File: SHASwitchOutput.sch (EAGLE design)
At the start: 39 parts, among them IC2 HLKPM01, Q1 2N7002, Q2 2N7002, Q3 2N7002, Q4 2N7002

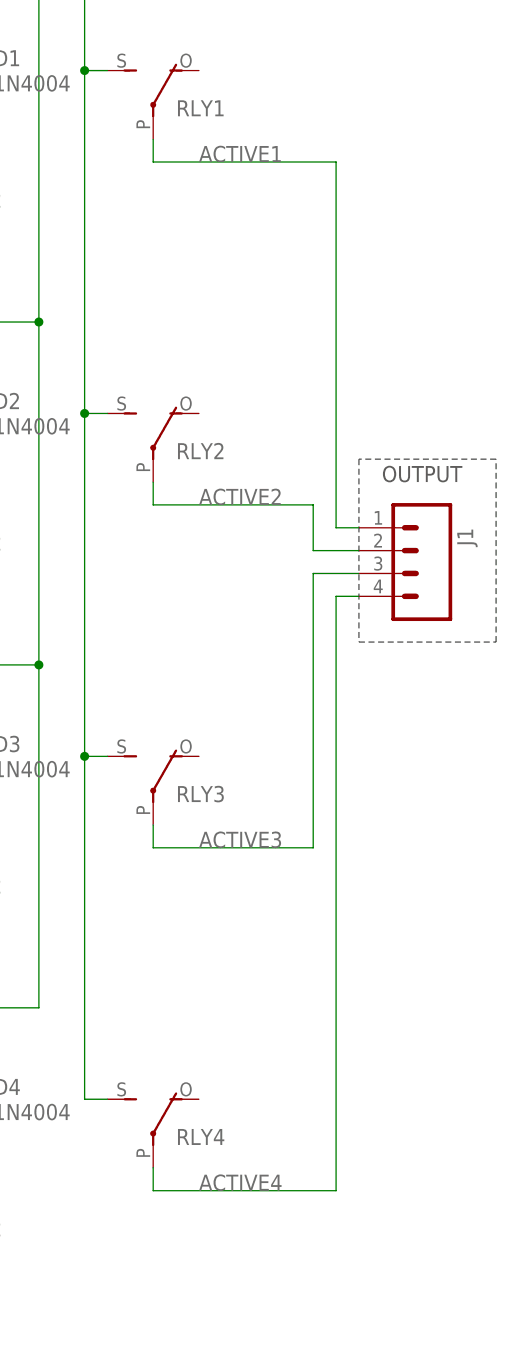
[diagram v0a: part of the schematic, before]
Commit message: Changed screw terminals from 3.5mm pitch to 5mm
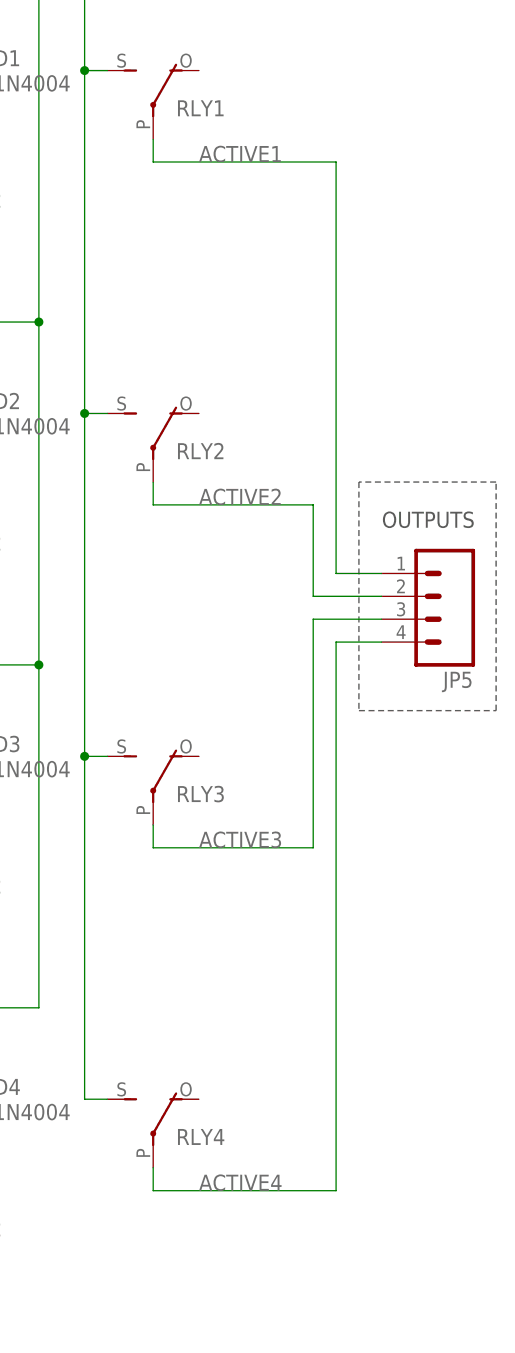
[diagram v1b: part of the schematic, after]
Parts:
- removed J1: (no value), freetronics-master-v1.1:M04SCREW
- added JP5: (no value), freetronics-jon:M045MM
- JP2: device freetronics-original:M03SCREW -> freetronics-jon:M035MM
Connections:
- net ACTIVE1: now also JP5.1; no longer J1.1
- net ACTIVE2: now also JP5.2; no longer J1.2
- net ACTIVE3: now also JP5.3; no longer J1.3
- net ACTIVE4: now also JP5.4; no longer J1.4
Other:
- note added: "OUTPUTS"
- note removed: "OUTPUT"
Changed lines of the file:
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@@
 <part name="GND12" library="SparkFun" deviceset="GND" device=""/>
 <part name="IC2" library="freetronics-jon" deviceset="HLKPM01" device=""/>
-<part name="J1" library="freetronics-master-v1.1" deviceset="M04" device="SCREW"/>
 <part name="GND2" library="SparkFun" deviceset="GND" device=""/>
 <part name="R2" library="freetronics" deviceset="RESISTOR" device="0603" value="330R"/>
@@
 <part name="JP1" library="freetronics-original" deviceset="M10" device="0.1"/>
 <part name="F1" library="freetronics-jon" deviceset="PICOFUSE" device="" value="250V 1A"/>
-<part name="JP2" library="freetronics-original" deviceset="M03" device="SCREW"/>
+<part name="JP2" library="freetronics-jon" deviceset="M03" device="5MM"/>
 <part name="GND14" library="SparkFun" deviceset="GND" device=""/>
 <part name="U$3" library="freetronics-original" deviceset="5V" device=""/>
+<part name="JP5" library="freetronics-jon" deviceset="M04" device="5MM"/>
 </parts>
 <sheets>
@@
 <frame x1="78.74" y1="5.08" x2="109.22" y2="10.16" columns="8" rows="5" layer="94"/>
 <frame x1="5.08" y1="5.08" x2="30.48" y2="10.16" columns="8" rows="5" layer="94"/>
-<wire x1="243.84" y1="114.3" x2="228.6" y2="114.3" width="0.1524" layer="97" style="shortdash"/>
-<wire x1="228.6" y1="114.3" x2="228.6" y2="93.98" width="0.1524" layer="97" style="shortdash"/>
-<wire x1="228.6" y1="93.98" x2="243.84" y2="93.98" width="0.1524" layer="97" style="shortdash"/>
-<wire x1="243.84" y1="93.98" x2="243.84" y2="114.3" width="0.1524" layer="97" style="shortdash"/>
-<text x="231.14" y="111.76" size="1.778" layer="97">OUTPUT</text>
+<wire x1="243.84" y1="111.76" x2="228.6" y2="111.76" width="0.1524" layer="97" style="shortdash"/>
+<wire x1="228.6" y1="111.76" x2="228.6" y2="86.36" width="0.1524" layer="97" style="shortdash"/>
+<wire x1="228.6" y1="86.36" x2="243.84" y2="86.36" width="0.1524" layer="97" style="shortdash"/>
+<wire x1="243.84" y1="86.36" x2="243.84" y2="111.76" width="0.1524" layer="97" style="shortdash"/>
+<text x="231.14" y="106.68" size="1.778" layer="97">OUTPUTS</text>
 </plain>
 <instances>
@@
 <instance part="GND12" gate="1" x="165.1" y="91.44"/>
 <instance part="IC2" gate="G$1" x="71.12" y="162.56"/>
-<instance part="J1" gate="G$1" x="233.68" y="104.14" smashed="yes" rot="R180">
-<attribute name="VALUE" x="238.76" y="111.76" size="1.778" layer="96" rot="R180"/>
-<attribute name="NAME" x="239.522" y="106.68" size="1.778" layer="95" rot="R270"/>
-</instance>
 <instance part="GND2" gate="1" x="137.16" y="48.26"/>
 <instance part="R2" gate="G$1" x="137.16" y="55.88" smashed="yes" rot="R90">
@@
 <instance part="GND14" gate="1" x="101.6" y="60.96"/>
 <instance part="U$3" gate="G$1" x="101.6" y="93.98"/>
+<instance part="JP5" gate="G$1" x="236.22" y="99.06" rot="R180"/>
 </instances>
 <busses>
@@
 <wire x1="205.74" y1="147.32" x2="205.74" y2="149.86" width="0.1524" layer="91"/>
 <label x="210.82" y="147.32" size="1.778" layer="95"/>
-<wire x1="226.06" y1="147.32" x2="226.06" y2="106.68" width="0.1524" layer="91"/>
-<pinref part="J1" gate="G$1" pin="1"/>
-<wire x1="226.06" y1="106.68" x2="228.6" y2="106.68" width="0.1524" layer="91"/>
+<wire x1="226.06" y1="147.32" x2="226.06" y2="101.6" width="0.1524" layer="91"/>
+<wire x1="231.14" y1="101.6" x2="226.06" y2="101.6" width="0.1524" layer="91"/>
+<pinref part="JP5" gate="G$1" pin="1"/>
 </segment>
 </net>
@@
 <wire x1="205.74" y1="109.22" x2="205.74" y2="111.76" width="0.1524" layer="91"/>
 <label x="210.82" y="109.22" size="1.778" layer="95"/>
-<wire x1="223.52" y1="109.22" x2="223.52" y2="104.14" width="0.1524" layer="91"/>
-<pinref part="J1" gate="G$1" pin="2"/>
-<wire x1="223.52" y1="104.14" x2="228.6" y2="104.14" width="0.1524" layer="91"/>
+<wire x1="223.52" y1="109.22" x2="223.52" y2="99.06" width="0.1524" layer="91"/>
+<wire x1="223.52" y1="99.06" x2="231.14" y2="99.06" width="0.1524" layer="91"/>
+<pinref part="JP5" gate="G$1" pin="2"/>
 </segment>
 </net>
@@
 <wire x1="205.74" y1="71.12" x2="205.74" y2="73.66" width="0.1524" layer="91"/>
 <label x="210.82" y="71.12" size="1.778" layer="95"/>
-<wire x1="223.52" y1="71.12" x2="223.52" y2="101.6" width="0.1524" layer="91"/>
-<pinref part="J1" gate="G$1" pin="3"/>
-<wire x1="223.52" y1="101.6" x2="228.6" y2="101.6" width="0.1524" layer="91"/>
+<wire x1="223.52" y1="71.12" x2="223.52" y2="96.52" width="0.1524" layer="91"/>
+<wire x1="223.52" y1="96.52" x2="231.14" y2="96.52" width="0.1524" layer="91"/>
+<pinref part="JP5" gate="G$1" pin="3"/>
 </segment>
 </net>
@@
 <wire x1="205.74" y1="33.02" x2="205.74" y2="35.56" width="0.1524" layer="91"/>
 <label x="210.82" y="33.02" size="1.778" layer="95"/>
-<wire x1="226.06" y1="33.02" x2="226.06" y2="99.06" width="0.1524" layer="91"/>
-<pinref part="J1" gate="G$1" pin="4"/>
-<wire x1="226.06" y1="99.06" x2="228.6" y2="99.06" width="0.1524" layer="91"/>
-</segment>
-</net>
+<wire x1="226.06" y1="33.02" x2="226.06" y2="93.98" width="0.1524" layer="91"/>
+<wire x1="226.06" y1="93.98" x2="231.14" y2="93.98" width="0.1524" layer="91"/>
+<pinref part="JP5" gate="G$1" pin="4"/>
+</segment>
+</net>

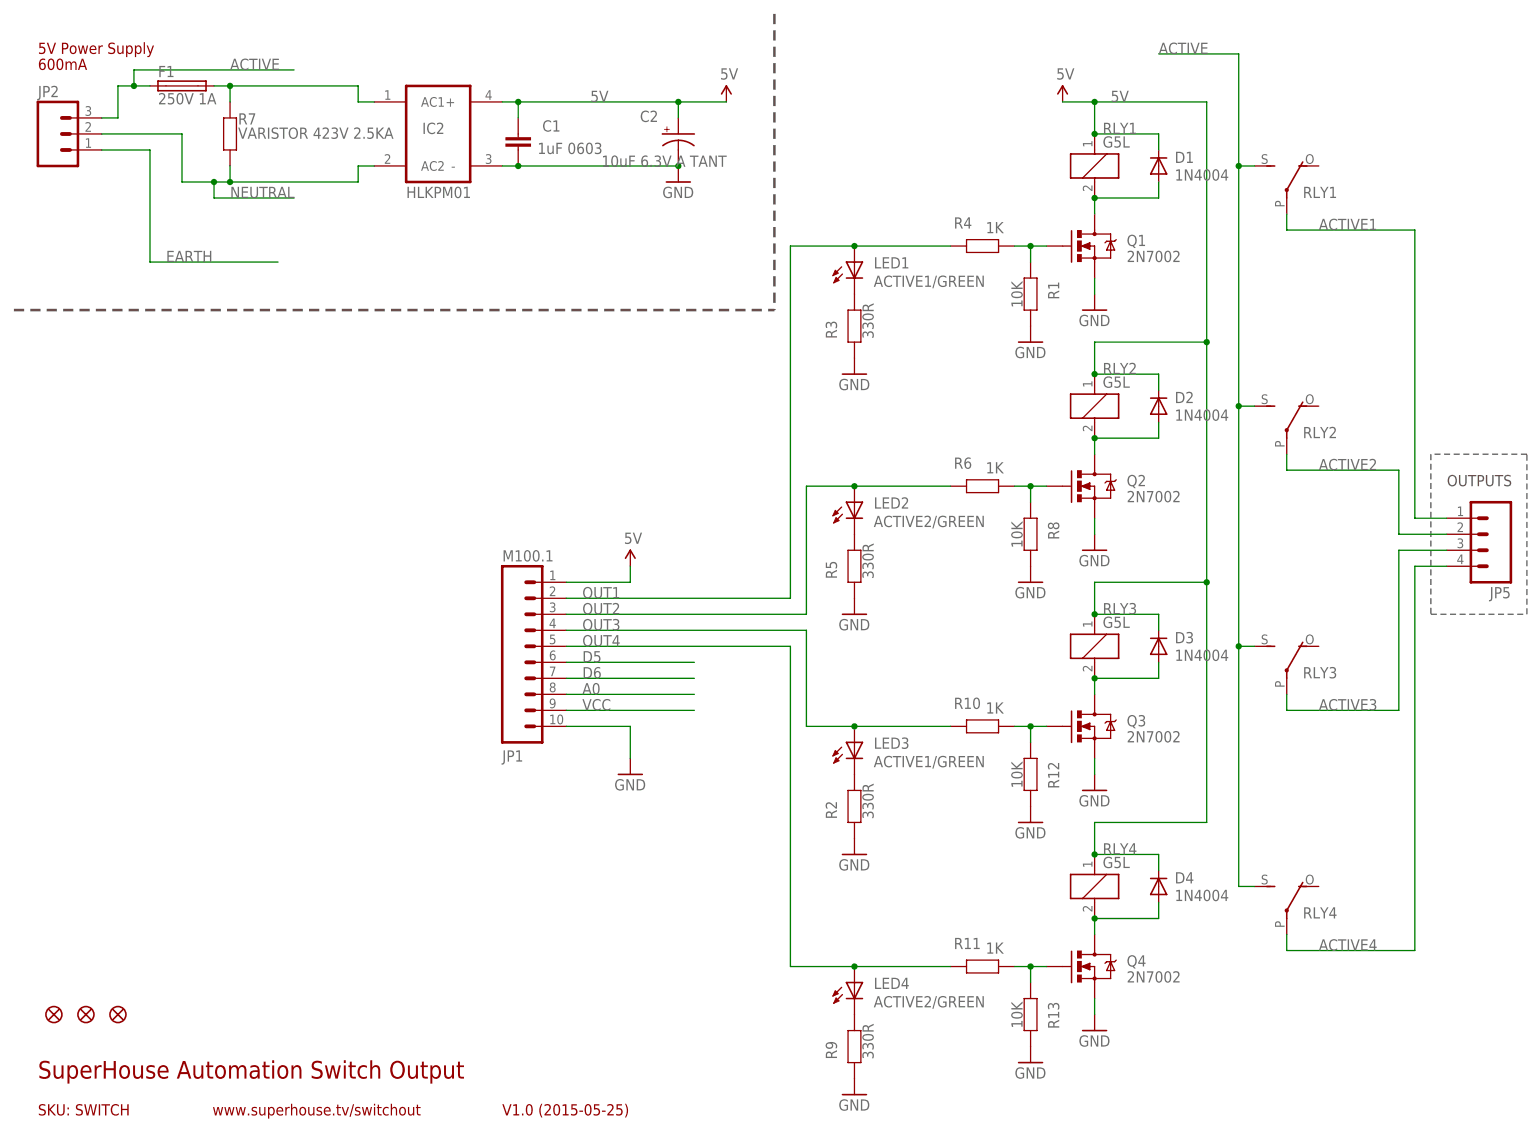
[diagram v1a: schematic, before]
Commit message: Added GND-Neutral solder jumper (normally open) Changed fuse to vertial orientation
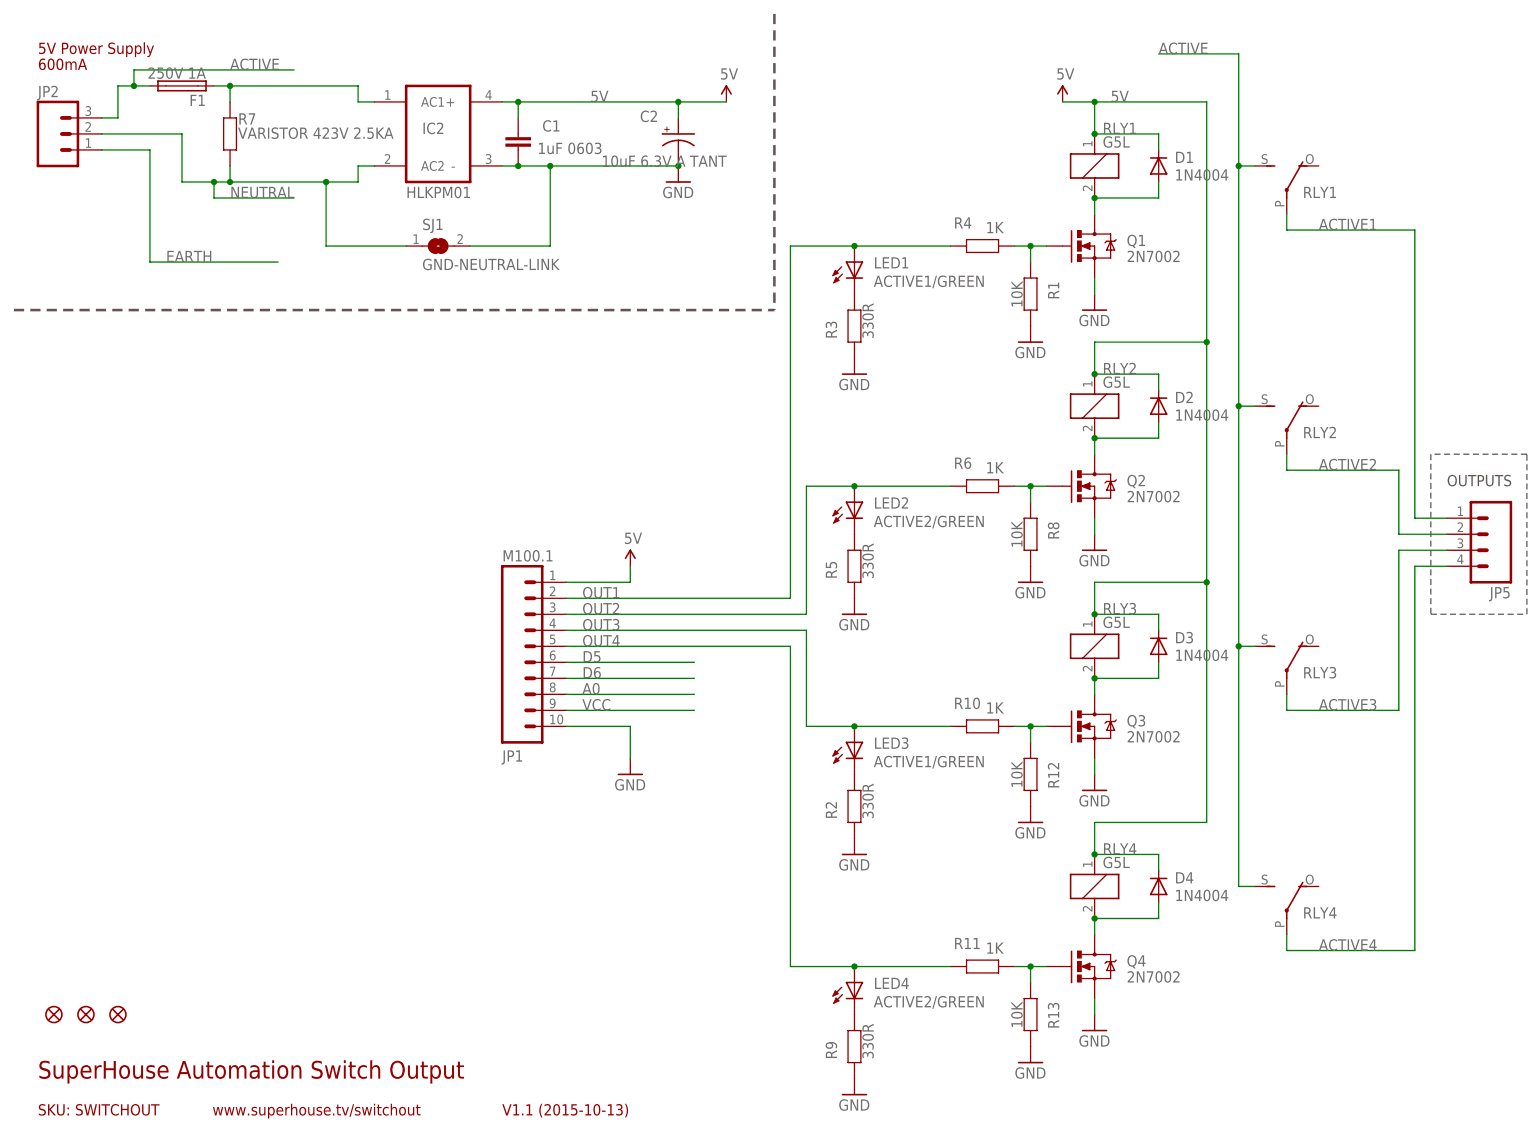
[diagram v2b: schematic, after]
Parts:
- added SJ1: GND-NEUTRAL-LINK, freetronics-jon:SJN
- F1: device freetronics-jon:PICOFUSE -> freetronics-jon:PICOFUSEV
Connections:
- net $N16: now also F1.1; no longer F1.2
- net ACTIVE: now also F1.2; no longer F1.1
- net GND: now also SJ1.2
- net NEUTRAL: now also SJ1.1
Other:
- note added: "SKU: SWITCHOUT"
- note added: "V1.1 (2015-10-13)"
- note removed: "SKU: SWITCH"
- note removed: "V1.0 (2015-05-25)"
- moved on the sheet: F1
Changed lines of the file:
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@@
 <part name="U$2" library="freetronics-original" deviceset="5V" device=""/>
 <part name="JP1" library="freetronics-original" deviceset="M10" device="0.1"/>
-<part name="F1" library="freetronics-jon" deviceset="PICOFUSE" device="" value="250V 1A"/>
+<part name="F1" library="freetronics-jon" deviceset="PICOFUSE" device="V" value="250V 1A"/>
 <part name="JP2" library="freetronics-jon" deviceset="M03" device="5MM"/>
 <part name="GND14" library="SparkFun" deviceset="GND" device=""/>
 <part name="U$3" library="freetronics-original" deviceset="5V" device=""/>
 <part name="JP5" library="freetronics-jon" deviceset="M04" device="5MM"/>
+<part name="SJ1" library="freetronics-jon" deviceset="SJ" device="N" value="GND-NEUTRAL-LINK"/>
 </parts>
 <sheets>
@@
 <wire x1="3.81" y1="134.62" x2="124.46" y2="134.62" width="0.4064" layer="97" style="longdash"/>
 <wire x1="124.46" y1="181.61" x2="124.46" y2="134.62" width="0.4064" layer="97" style="longdash"/>
-<text x="7.62" y="6.858" size="1.778" layer="94">SKU: SWITCH</text>
+<text x="7.62" y="6.858" size="1.778" layer="94">SKU: SWITCHOUT</text>
 <text x="7.62" y="175.26" size="1.778" layer="94">5V Power Supply</text>
 <text x="7.62" y="172.72" size="1.778" layer="94">600mA</text>
 <text x="7.62" y="12.7" size="2.794" layer="94">SuperHouse Automation Switch Output</text>
-<text x="81.28" y="6.858" size="1.778" layer="94">V1.0 (2015-05-25)</text>
+<text x="81.28" y="6.858" size="1.778" layer="94">V1.1 (2015-10-13)</text>
 <text x="35.306" y="6.858" size="1.778" layer="94">www.superhouse.tv/switchout</text>
 <frame x1="0" y1="0" x2="248.92" y2="185.42" columns="8" rows="5" layer="94"/>
@@
 <instance part="U$2" gate="G$1" x="170.18" y="167.64"/>
 <instance part="JP1" gate="G$1" x="81.28" y="73.66" rot="MR180"/>
-<instance part="F1" gate="1" x="30.48" y="170.18"/>
+<instance part="F1" gate="1" x="30.48" y="170.18" rot="R180"/>
 <instance part="JP2" gate="G$1" x="10.16" y="162.56"/>
 <instance part="GND14" gate="1" x="101.6" y="60.96"/>
 <instance part="U$3" gate="G$1" x="101.6" y="93.98"/>
 <instance part="JP5" gate="G$1" x="236.22" y="99.06" rot="R180"/>
+<instance part="SJ1" gate="1" x="71.12" y="144.78"/>
 </instances>
 <busses>
@@
 <net name="GND" class="0">
 <segment>
-<wire x1="83.82" y1="157.48" x2="109.22" y2="157.48" width="0.1524" layer="91"/>
+<wire x1="83.82" y1="157.48" x2="88.9" y2="157.48" width="0.1524" layer="91"/>
 <junction x="83.82" y="157.48"/>
 <pinref part="C2" gate="G$1" pin="-"/>
 <pinref part="C1" gate="G$1" pin="2"/>
+<wire x1="88.9" y1="157.48" x2="109.22" y2="157.48" width="0.1524" layer="91"/>
 <wire x1="81.28" y1="157.48" x2="83.82" y2="157.48" width="0.1524" layer="91"/>
 <pinref part="GND10" gate="1" pin="GND"/>
 <junction x="109.22" y="157.48"/>
 <pinref part="IC2" gate="G$1" pin="-"/>
+<pinref part="SJ1" gate="1" pin="2"/>
+<wire x1="76.2" y1="144.78" x2="88.9" y2="144.78" width="0.1524" layer="91"/>
+<wire x1="88.9" y1="144.78" x2="88.9" y2="157.48" width="0.1524" layer="91"/>
+<junction x="88.9" y="157.48"/>
 </segment>
 <segment>
@@
 <wire x1="38.1" y1="157.48" x2="38.1" y2="154.94" width="0.1524" layer="91"/>
 <junction x="38.1" y="154.94"/>
-<wire x1="58.42" y1="154.94" x2="38.1" y2="154.94" width="0.1524" layer="91"/>
+<wire x1="58.42" y1="154.94" x2="53.34" y2="154.94" width="0.1524" layer="91"/>
 <pinref part="R7" gate="G$1" pin="1"/>
+<wire x1="53.34" y1="154.94" x2="38.1" y2="154.94" width="0.1524" layer="91"/>
 <wire x1="35.56" y1="154.94" x2="30.48" y2="154.94" width="0.1524" layer="91"/>
 <wire x1="30.48" y1="154.94" x2="30.48" y2="162.56" width="0.1524" layer="91"/>
@@
 <pinref part="IC2" gate="G$1" pin="AC2"/>
 <wire x1="58.42" y1="157.48" x2="60.96" y2="157.48" width="0.1524" layer="91"/>
+<pinref part="SJ1" gate="1" pin="1"/>
+<wire x1="66.04" y1="144.78" x2="53.34" y2="144.78" width="0.1524" layer="91"/>
+<wire x1="53.34" y1="144.78" x2="53.34" y2="154.94" width="0.1524" layer="91"/>
+<junction x="53.34" y="154.94"/>
 </segment>
 </net>
@@
 <wire x1="20.32" y1="165.1" x2="17.78" y2="165.1" width="0.1524" layer="91"/>
 <label x="38.1" y="172.72" size="1.778" layer="95"/>
-<pinref part="F1" gate="1" pin="1"/>
-<wire x1="22.86" y1="170.18" x2="25.4" y2="170.18" width="0.1524" layer="91"/>
+<pinref part="JP2" gate="G$1" pin="3"/>
+<pinref part="F1" gate="1" pin="2"/>
+<wire x1="25.4" y1="170.18" x2="22.86" y2="170.18" width="0.1524" layer="91"/>
 <junction x="22.86" y="170.18"/>
-<pinref part="JP2" gate="G$1" pin="3"/>
 </segment>
 </net>
@@
 <pinref part="R7" gate="G$1" pin="2"/>
 <wire x1="38.1" y1="167.64" x2="38.1" y2="170.18" width="0.1524" layer="91"/>
-<pinref part="F1" gate="1" pin="2"/>
-<wire x1="38.1" y1="170.18" x2="35.56" y2="170.18" width="0.1524" layer="91"/>
-<junction x="38.1" y="170.18"/>
 <wire x1="58.42" y1="170.18" x2="58.42" y2="167.64" width="0.1524" layer="91"/>
 <pinref part="IC2" gate="G$1" pin="AC1"/>
 <wire x1="58.42" y1="167.64" x2="60.96" y2="167.64" width="0.1524" layer="91"/>
-</segment>
-</net>
+<pinref part="F1" gate="1" pin="1"/>
+<wire x1="38.1" y1="170.18" x2="35.56" y2="170.18" width="0.1524" layer="91"/>
+<junction x="38.1" y="170.18"/>
+</segment>
+</net>
